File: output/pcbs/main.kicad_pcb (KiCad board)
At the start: 2 copper layers, 141 x 130.1 mm, 62 parts

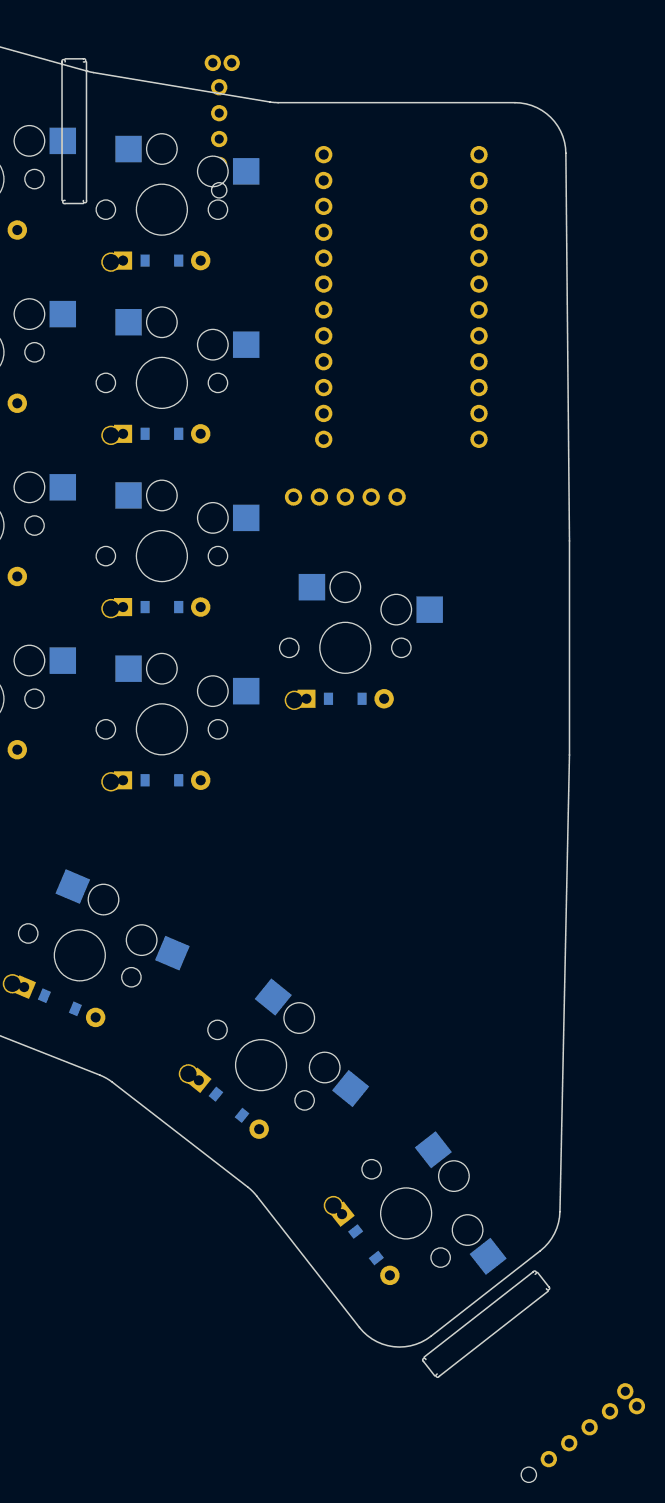
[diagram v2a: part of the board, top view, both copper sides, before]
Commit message: Wire encoder 1 push-switch into the key matrix
- Add the EVQWGD001 push-switch (pins 1&2) to the matrix on the free
  intersection column P15 (single) x row P11 (num), via node ENC1_SW, with a
  dedicated diode (ENC1_SW -> P11)
- Rotary A/C stay on nice!nano P0/P1; B/D on GND
- Only one encoder (encoder 2 not added)
- Regenerated output/
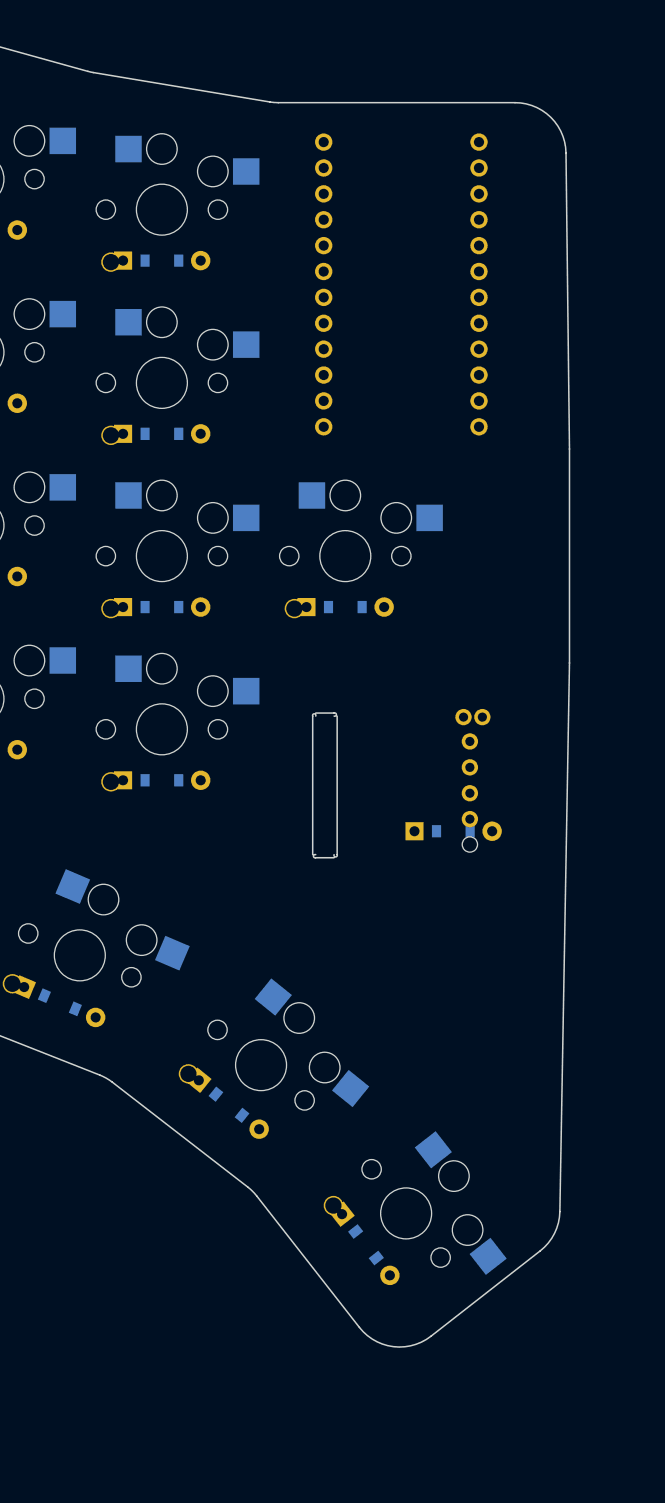
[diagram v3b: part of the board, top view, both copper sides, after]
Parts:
- removed DISP1: , ceoloide:display_nice_view
- removed ENC2: , ceoloide:encoder_evqwgd001
- added D30: , ceoloide:diode_tht_sod123, B.Cu at (144.6, 94.5)
- moved ENC1 61.2 mm to (140.6, 89.5), turned to 0 degrees
- moved D25 9.00 mm to (134.0, 72.5)
- moved S25 9.00 mm to (134.0, 67.5)
- moved MCU1 1.23 mm to (139.5, 39.6)
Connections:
- ENC1 pad 1: GND -> P15
- ENC1 pad 2: GND -> ENC1_SW
- MCU1 pad 13: ENC2_C -> P10
- MCU1 pad 5: ENC2_A -> P2
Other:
- outline, holes or cut-outs redrawn

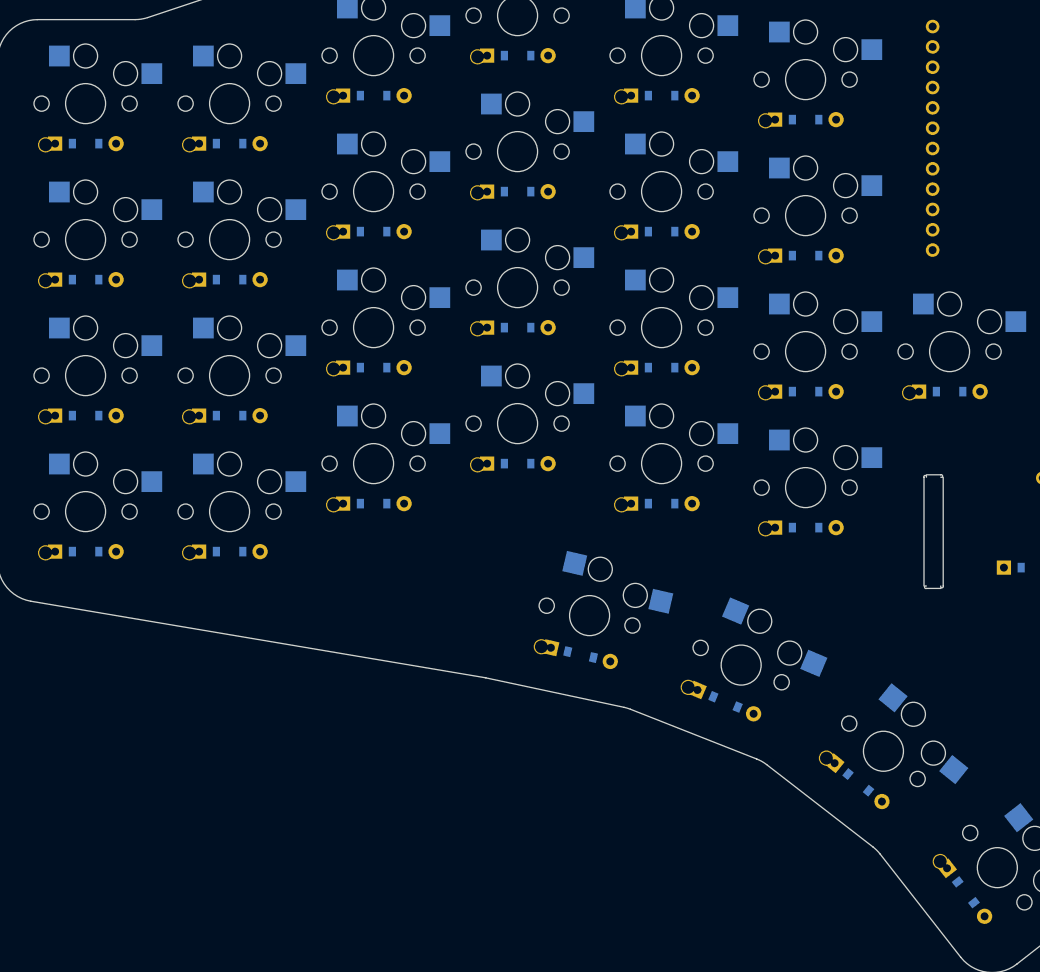
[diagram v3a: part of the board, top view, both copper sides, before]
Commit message: Wiring audit fixes: connect thumb keys, remove nice!view
- FIX: the 4 thumb cluster keys (inner/home/outer/oouter) had no column_net
  or row_net, leaving them electrically floating (dead keys). Assign columns
  P16-P19 and a new row P2 (nice!nano pin 5), giving each a unique intersection
- Remove nice!view display (per user) and its now-unused SPI pin assignments
  (MOSI/SCK/CS on P8/P9/P3)
- Audit result: 30 keys / 30 diodes / 30 unique col x row intersections,
  no MCU pin conflicts, no floating matrix nodes, encoder rotary+switch verified
- Regenerated output/
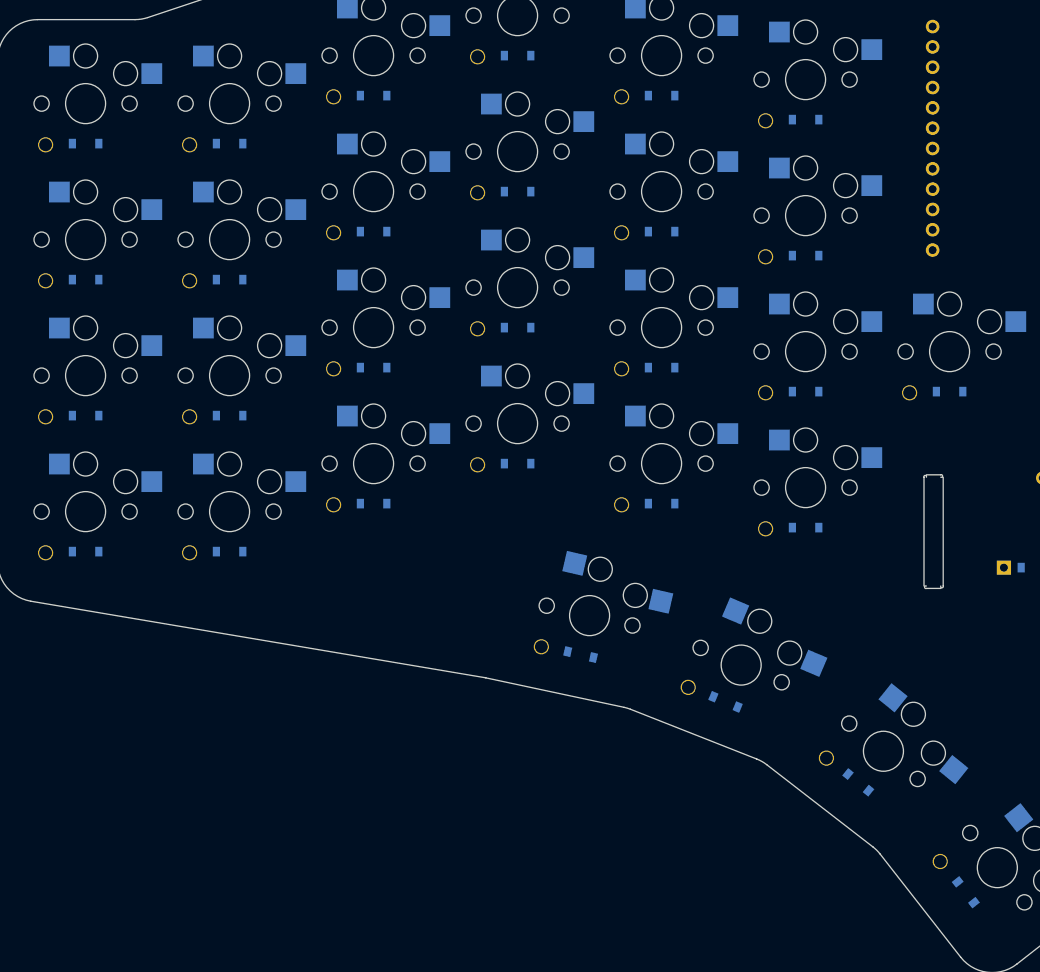
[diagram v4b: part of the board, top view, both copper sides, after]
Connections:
- net CS renamed P3
- net MOSI renamed P8
- net SCK renamed P9
- D26 pad 1: (no net) -> P2
- D27 pad 1: (no net) -> P2
- D28 pad 1: (no net) -> P2
- D29 pad 1: (no net) -> P2
- S26 pad 1: (no net) -> P16
- S27 pad 1: (no net) -> P17
- S28 pad 1: (no net) -> P18
- S29 pad 1: (no net) -> P19

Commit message: Add reset button, power switch, battery connector, mounting holes
- Vendor 4 KiCad 8 footprints: reset_switch_tht_top, power_switch_smd_side,
  battery_connector_jst_ph_2, mounting_hole_plated
- Power path: Battery BAT_P -> power switch -> nice!nano RAW; BAT_N -> GND
- Reset button: RST -> GND (no GPIO used)
- 4 M2 plated mounting holes near board corners
- Placeholder positions (adjust where: to taste)
- Audit: power path + reset connectivity verified; matrix still 30 keys /
  30 diodes / 30 unique intersections, no conflicts
- Regenerated output/
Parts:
- added H1: , ceoloide:mounting_hole_plated, B.Cu at (21.6, 32.3)
- added H2: , ceoloide:mounting_hole_plated, B.Cu at (129.2, 29.3)
- added H3: , ceoloide:mounting_hole_plated, B.Cu at (21.6, 91.7)
- added H4: , ceoloide:mounting_hole_plated, B.Cu at (139.1, 141.1)
- added JST1: , ceoloide:battery_connector_jst_ph_2, B.Cu at (134.0, 19.2)
- added PWR1: , ceoloide:power_switch_smd_side, B.Cu at (112.0, 19.2)
- added RST1: , ceoloide:reset_switch_tht_top, B.Cu at (156.0, 19.2)
